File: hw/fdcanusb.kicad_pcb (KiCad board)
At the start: 4 copper layers, 30 x 18 mm, 33 parts, among them J1 Conn_01x03, J2 216990-0002, U1 STM32G474CEU6, U2 TCAN1057AEVDRQ1, U3 TLP3317, U4 USBLC6-2SC6, U5 TLV70233DSER

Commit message: WIP - nearly all routing complete
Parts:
- C2: moved to B.Cu
- moved C2 8.36 mm to (143.0, 105.5), turned to 90 degrees
- moved C6 7.94 mm to (139.8, 105.7)
- moved R1 7.31 mm to (143.8, 96.5)
- moved C7 6.12 mm to (137.3, 97.6), turned to 90 degrees
- moved U3 3.19 mm to (146.8, 98.8), turned to 0 degrees
- moved U1 2.76 mm to (134.3, 103.2), turned to 90 degrees
- moved C12 2.54 mm to (128.8, 99.5), turned to 180 degrees
- moved R2 2.30 mm to (146.8, 102.0)
- moved C3 2.23 mm to (128.8, 104.0), turned to 180 degrees
- moved R5 2.20 mm to (148.1, 93.7), turned to 180 degrees
- moved R6 2.19 mm to (148.2, 106.2), turned to 180 degrees
- moved C5 2.11 mm to (128.8, 101.0), turned to 180 degrees
- moved C4 1.88 mm to (128.8, 102.5), turned to 180 degrees
- moved D3 1.84 mm to (131.2, 92.3), turned to 0 degrees
- moved U4 1.24 mm to (130.3, 96.8)
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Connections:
- net Net-(J1-Pin_1) renamed /CAN/CAN_P
- net Net-(J1-Pin_2) renamed /CAN/CAN_N
- net Net-(J2-DN1) renamed /Power Input/USB_N
- net Net-(J2-DP1) renamed /Power Input/USB_P
- U1 pad 41: /stm32g4/LED_CAN_TX -> /LED Debug/LED_CAN_TX
- U1 pad 42: /stm32g4/LED_CAN_RX -> /LED Debug/LED_CAN_RX
- U1 pad 43: /stm32g4/LED_PWR -> /LED Debug/LED_PWR
- U1 pad 44: /stm32g4/LED_COM -> /LED Debug/LED_COM
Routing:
- net /LED Debug/LED_PWR: track 0.00 -> 43.1 mm, vias 0 -> 1
- net /LED Debug/LED_COM: track 0.00 -> 39.2 mm, vias 0 -> 1
- net +5V: track 0.00 -> 32.9 mm, vias 0 -> 1
- net GND: track 0.00 -> 31.3 mm, vias 0 -> 23
- net +3V: track 0.00 -> 23.7 mm, vias 0 -> 8
- net /CAN/CAN_TERM: track 0.00 -> 20.7 mm
- net /CAN/CAN_N: track 0.00 -> 17.0 mm, vias 0 -> 1
- net /CAN/CAN_P: track 0.00 -> 17.0 mm, vias 0 -> 1
- net /LED Debug/LED_CAN_TX: track 0.00 -> 16.3 mm, vias 0 -> 1
- net /stm32g4/NRST: track 0.00 -> 14.1 mm, vias 0 -> 2
- net /stm32g4/SWDIO: track 0.00 -> 13.9 mm, vias 0 -> 1
- net /Power Input/USB_N: track 0.00 -> 12.4 mm, vias 0 -> 2
- net /Power Input/USB_F_P: track 0.00 -> 11.7 mm, vias 0 -> 1
- net /Power Input/USB_P: track 0.00 -> 11.6 mm, vias 0 -> 2
- net /stm32g4/SWCLK: track 0.00 -> 11.4 mm, vias 0 -> 1
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- added copper zone on B.Cu, net GND
- added copper zone on F.Cu, net GND
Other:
- board text added: "SWD"

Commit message: Maybe complete routing and passes all DRC
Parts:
- moved C11 0.25 mm to (124.9, 97.5)
- moved D3 0.10 mm to (131.3, 92.3)
- moved R8 0.10 mm to (128.9, 93.6)
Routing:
- net +3V: track 23.7 -> 28.7 mm, vias 8 -> 12
- net GND: track 31.3 -> 34.3 mm, vias 23 -> 27
- added copper zone on F.Cu, net +3V
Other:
- board text added: "G"
- board text added: "H"
- board text added: "L"

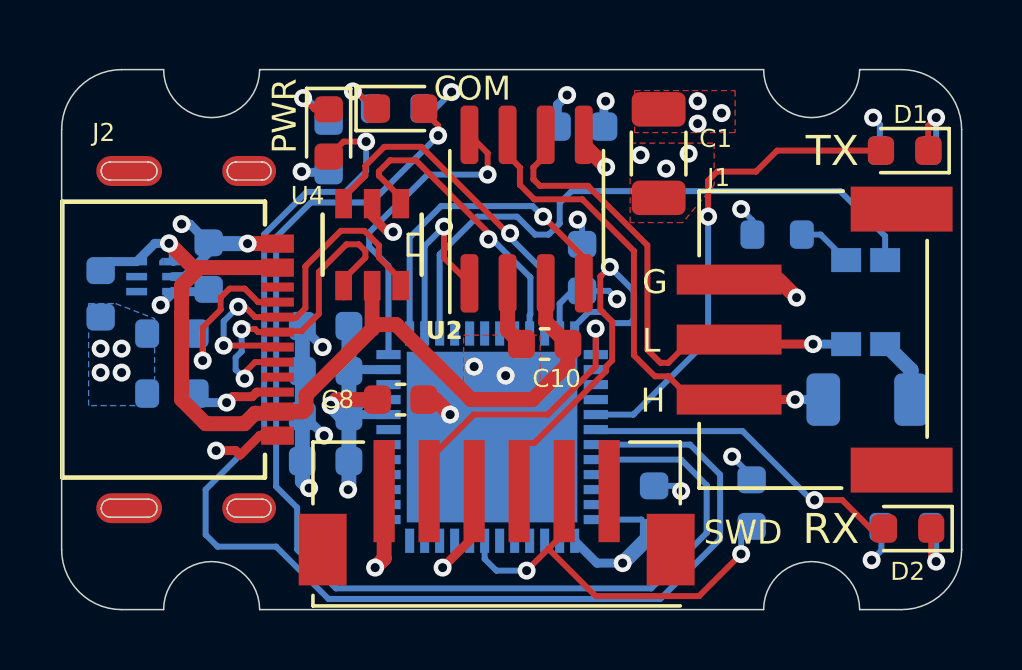
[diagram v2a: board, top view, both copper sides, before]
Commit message: r4: Add board label and fine silk tune
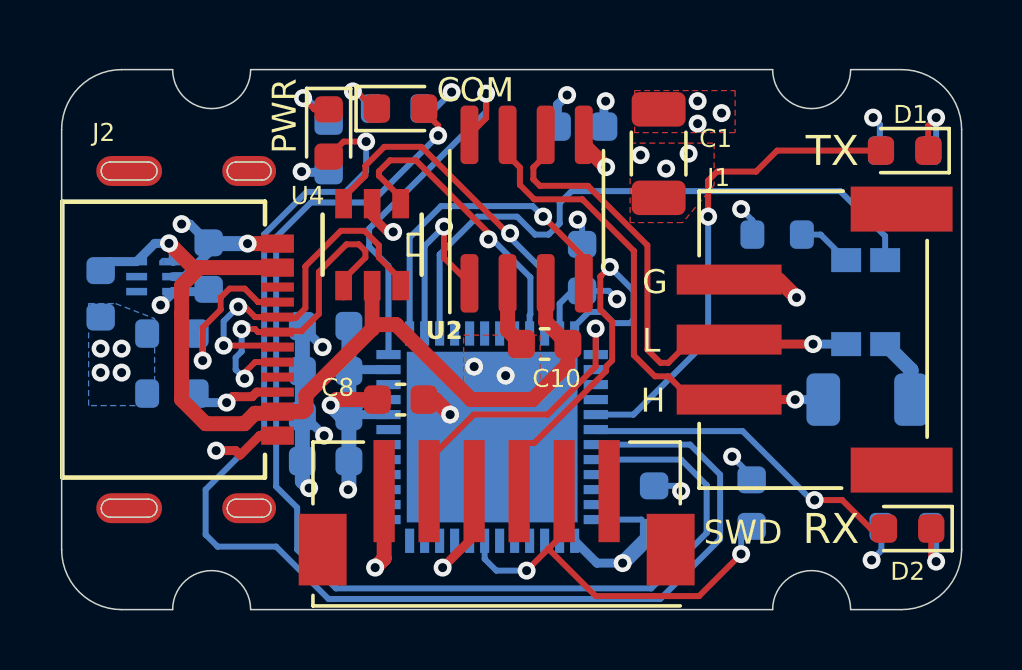
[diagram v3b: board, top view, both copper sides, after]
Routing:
- net /CAN/CAN_STB: track 10.7 -> 12.2 mm
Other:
- outline, holes or cut-outs redrawn
- board text added: "(c) 2023"
- board text added: "fdcanusb r4"

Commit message: r4: More work to get silk off vias
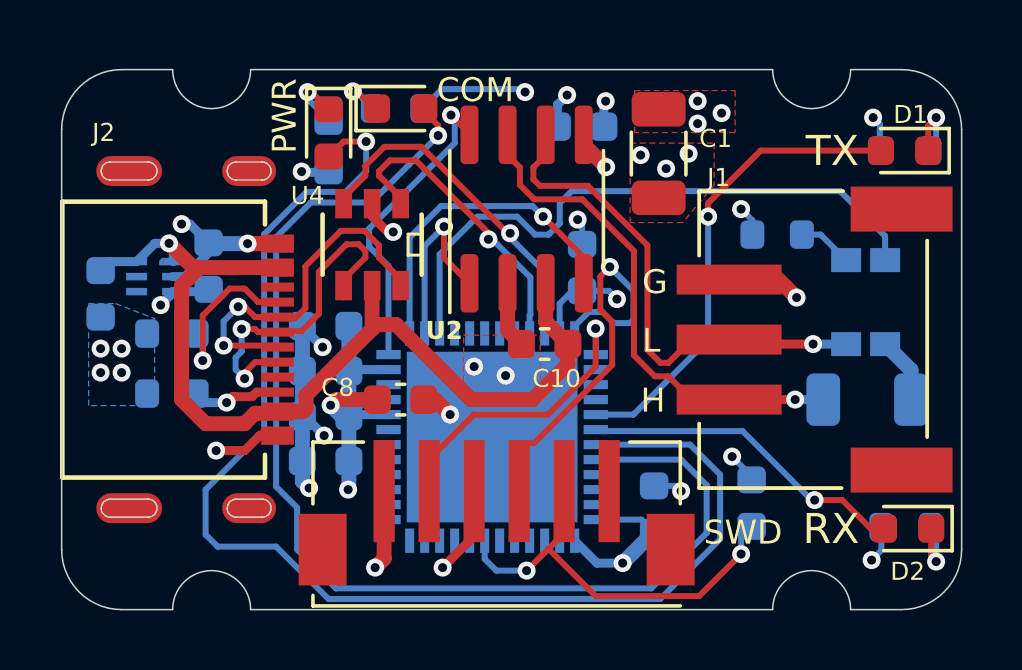
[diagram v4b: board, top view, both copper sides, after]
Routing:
- net GND: track 34.3 -> 36.7 mm
- net /CAN/CAN_STB: track 12.2 -> 10.4 mm

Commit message: Add debug pads for power rails
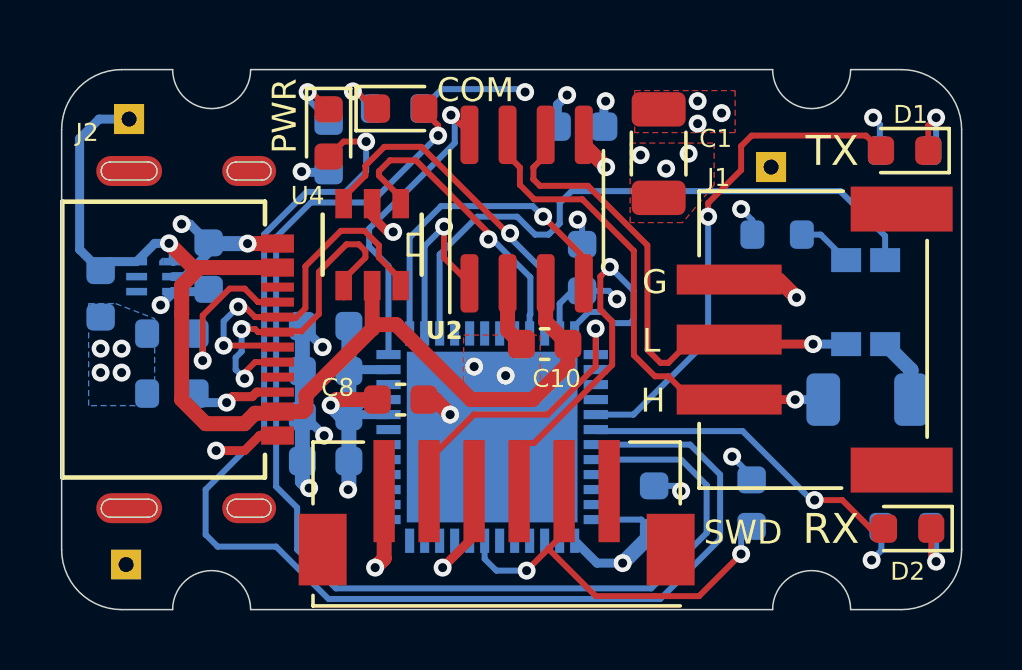
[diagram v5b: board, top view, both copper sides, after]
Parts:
- added J3: Conn_01x01, TestPoint:TestPoint_THTPad_1.0x1.0mm_Drill0.5mm, B.Cu at (122.2, 107.5)
- added J4: Conn_01x01, TestPoint:TestPoint_THTPad_1.0x1.0mm_Drill0.5mm, B.Cu at (143.7, 94.2)
- added J5: Conn_01x01, TestPoint:TestPoint_THTPad_1.0x1.0mm_Drill0.5mm, B.Cu at (122.2, 92.7)
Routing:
- net +5V: track 32.7 -> 39.4 mm
- net /LED Debug/LED_CAN_TX: track 15.8 -> 16.7 mm
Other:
- board text added: "3"
- board text added: "5"
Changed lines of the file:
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@@
     (property "ki_keywords" "216990-0002")
     (attr smd)
-    (fp_text reference "J2" (at -6.9 2 unlocked) (layer "F.SilkS")
+    (fp_text reference "J2" (at -6.9 2.55 unlocked) (layer "F.SilkS")
         (effects (font (size 0.6 0.6) (thickness 0.1)))
     )
@@
     )
   )
+  (footprint "TestPoint:TestPoint_THTPad_1.0x1.0mm_Drill0.5mm" (layer "B.Cu")
+    (at 143.65 94.25 180)
+    (descr "THT rectangular pad as test Point, square 1.0mm side length, hole diameter 0.5mm")
+    (tags "test point THT pad rectangle square")
+    (property "Sheetfile" "led_debug.kicad_sch")
+    (property "Sheetname" "LED Debug")
+    (property "exclude_from_bom" "")
+    (property "ki_description" "Generic connector, single row, 01x01, script generated (kicad-library-utils/schlib/autogen/connector/)")
+    (property "ki_keywords" "connector")
+    (attr exclude_from_pos_files exclude_from_bom)
+    (fp_text reference "J4" (at 0 1.448) (layer "B.SilkS") hide
+        (effects (font (size 1 1) (thickness 0.15)) (justify mirror))
+    )
+    (fp_text value "Conn_01x01" (at 0 -1.55) (layer "B.Fab") hide
+        (effects (font (size 1 1) (thickness 0.15)) (justify mirror))
+    )
+    (fp_line (start -0.7 -0.7) (end -0.7 0.7)
+      (stroke (width 0.12) (type solid)) (layer "B.SilkS"))
+    (fp_line (start -0.7 0.7) (end 0.7 0.7)
+      (stroke (width 0.12) (type solid)) (layer "B.SilkS"))
+    (fp_line (start 0.7 -0.7) (end -0.7 -0.7)
+      (stroke (width 0.12) (type solid)) (layer "B.SilkS"))
+    (fp_line (start 0.7 0.7) (end 0.7 -0.7)
+      (stroke (width 0.12) (type solid)) (layer "B.SilkS"))
+    (fp_line (start -1 1) (end -1 -1)
+      (stroke (width 0.05) (type solid)) (layer "B.CrtYd"))
+    (fp_line (start -1 1) (end 1 1)
+      (stroke (width 0.05) (type solid)) (layer "B.CrtYd"))
+    (fp_line (start 1 -1) (end -1 -1)
+      (stroke (width 0.05) (type solid)) (layer "B.CrtYd"))
+    (fp_line (start 1 -1) (end 1 1)
+      (stroke (width 0.05) (type solid)) (layer "B.CrtYd"))
+    (pad "1" thru_hole rect (at 0 0 180) (size 1 1) (drill 0.5) (layers "*.Cu" "*.Mask")
+      (net 1 "+3V") (pinfunction "Pin_1") (pintype "passive"))
+  )
+  (footprint "TestPoint:TestPoint_THTPad_1.0x1.0mm_Drill0.5mm" (layer "B.Cu")
+    (at 122.15 107.5 180)
+    (descr "THT rectangular pad as test Point, square 1.0mm side length, hole diameter 0.5mm")
+    (tags "test point THT pad rectangle square")
+    (property "Sheetfile" "led_debug.kicad_sch")
+    (property "Sheetname" "LED Debug")
+    (property "exclude_from_bom" "")
+    (property "ki_description" "Generic connector, single row, 01x01, script generated (kicad-library-utils/schlib/autogen/connector/)")
+    (property "ki_keywords" "connector")
+    (attr exclude_from_pos_files exclude_from_bom)
+    (fp_text reference "J3" (at 0 1.448) (layer "B.SilkS") hide
+        (effects (font (size 1 1) (thickness 0.15)) (justify mirror))
+    )
+    (fp_text value "Conn_01x01" (at 0 -1.55) (layer "B.Fab") hide
+        (effects (font (size 1 1) (thickness 0.15)) (justify mirror))
+    )
+    (fp_line (start -0.7 -0.7) (end -0.7 0.7)
+      (stroke (width 0.12) (type solid)) (layer "B.SilkS"))
+    (fp_line (start -0.7 0.7) (end 0.7 0.7)
+      (stroke (width 0.12) (type solid)) (layer "B.SilkS"))
+    (fp_line (start 0.7 -0.7) (end -0.7 -0.7)
+      (stroke (width 0.12) (type solid)) (layer "B.SilkS"))
+    (fp_line (start 0.7 0.7) (end 0.7 -0.7)
+      (stroke (width 0.12) (type solid)) (layer "B.SilkS"))
+    (fp_line (start -1 1) (end -1 -1)
+      (stroke (width 0.05) (type solid)) (layer "B.CrtYd"))
+    (fp_line (start -1 1) (end 1 1)
+      (stroke (width 0.05) (type solid)) (layer "B.CrtYd"))
+    (fp_line (start 1 -1) (end -1 -1)
+      (stroke (width 0.05) (type solid)) (layer "B.CrtYd"))
+    (fp_line (start 1 -1) (end 1 1)
+      (stroke (width 0.05) (type solid)) (layer "B.CrtYd"))
+    (pad "1" thru_hole rect (at 0 0 180) (size 1 1) (drill 0.5) (layers "*.Cu" "*.Mask")
+      (net 2 "GND") (pinfunction "Pin_1") (pintype "passive"))
+  )
   (footprint "Resistor_SMD:R_0603_1608Metric" (layer "B.Cu")
     (at 143.85 96.5)
@@
     )
   )
+  (footprint "TestPoint:TestPoint_THTPad_1.0x1.0mm_Drill0.5mm" (layer "B.Cu")
+    (at 122.25 92.65 180)
+    (descr "THT rectangular pad as test Point, square 1.0mm side length, hole diameter 0.5mm")
+    (tags "test point THT pad rectangle square")
+    (property "Sheetfile" "led_debug.kicad_sch")
+    (property "Sheetname" "LED Debug")
+    (property "exclude_from_bom" "")
+    (property "ki_description" "Generic connector, single row, 01x01, script generated (kicad-library-utils/schlib/autogen/connector/)")
+    (property "ki_keywords" "connector")
+    (attr exclude_from_pos_files exclude_from_bom)
+    (fp_text reference "J5" (at 0 1.448) (layer "B.SilkS") hide
+        (effects (font (size 1 1) (thickness 0.15)) (justify mirror))
+    )
+    (fp_text value "Conn_01x01" (at 0 -1.55) (layer "B.Fab") hide
+        (effects (font (size 1 1) (thickness 0.15)) (justify mirror))
+    )
+    (fp_line (start -0.7 -0.7) (end -0.7 0.7)
+      (stroke (width 0.12) (type solid)) (layer "B.SilkS"))
+    (fp_line (start -0.7 0.7) (end 0.7 0.7)
+      (stroke (width 0.12) (type solid)) (layer "B.SilkS"))
+    (fp_line (start 0.7 -0.7) (end -0.7 -0.7)
+      (stroke (width 0.12) (type solid)) (layer "B.SilkS"))
+    (fp_line (start 0.7 0.7) (end 0.7 -0.7)
+      (stroke (width 0.12) (type solid)) (layer "B.SilkS"))
+    (fp_line (start -1 1) (end -1 -1)
+      (stroke (width 0.05) (type solid)) (layer "B.CrtYd"))
+    (fp_line (start -1 1) (end 1 1)
+      (stroke (width 0.05) (type solid)) (layer "B.CrtYd"))
+    (fp_line (start 1 -1) (end -1 -1)
+      (stroke (width 0.05) (type solid)) (layer "B.CrtYd"))
+    (fp_line (start 1 -1) (end 1 1)
+      (stroke (width 0.05) (type solid)) (layer "B.CrtYd"))
+    (pad "1" thru_hole rect (at 0 0 180) (size 1 1) (drill 0.5) (layers "*.Cu" "*.Mask")
+      (net 4 "+5V") (pinfunction "Pin_1") (pintype "passive"))
+  )
   (footprint "Capacitor_SMD:C_0603_1608Metric" (layer "B.Cu")
     (at 128.8 104.05 180)
@@
   (gr_line (start 126.3 91) (end 143.7 91)
     (stroke (width 0.05) (type default)) (layer "Edge.Cuts"))
+  (gr_text "G" (at 124.1 107.75) (layer "B.SilkS")
+    (effects (font (size 0.8 0.8) (thickness 0.125)) (justify left bottom mirror))
+  )
+  (gr_text "3" (at 145.6 94.75) (layer "B.SilkS")
+    (effects (font (size 0.8 0.8) (thickness 0.125)) (justify left bottom mirror))
+  )
   (gr_text "(c) 2023" (at 133.7 97.75) (layer "B.SilkS")
     (effects (font (size 0.8 0.8) (thickness 0.125)) (justify left bottom mirror))
@@
     (effects (font (size 0.8 0.8) (thickness 0.125)) (justify left bottom mirror))
   )
+  (gr_text "5" (at 124.15 93.2) (layer "B.SilkS")
+    (effects (font (size 0.8 0.8) (thickness 0.125)) (justify left bottom mirror))
+  )
   (gr_text "G" (at 139.35 98.55) (layer "F.SilkS")
     (effects (font (size 0.8 0.8) (thickness 0.125)) (justify left bottom))
@@
   (segment (start 121.599998 97.400002) (end 121.3 97.7) (width 0.3) (layer "B.Cu") (net 4))
   (segment (start 123.720002 97.400002) (end 123.720002 96.931164) (width 0.3) (layer "B.Cu") (net 4))
+  (segment (start 120.6 97) (end 120.6 93.3) (width 0.3) (layer "B.Cu") (net 4))
+  (segment (start 120.6 93.3) (end 121.25 92.65) (width 0.3) (layer "B.Cu") (net 4))
+  (segment (start 121.3 97.7) (end 120.6 97) (width 0.3) (layer "B.Cu") (net 4))
+  (segment (start 121.25 92.65) (end 122.25 92.65) (width 0.3) (layer "B.Cu") (net 4))
   (segment (start 148.8875 92.8625) (end 149.15 92.6) (width 0.2) (layer "F.Cu") (net 5))
   (segment (start 148.8875 93.7) (end 148.8875 92.8625) (width 0.2) (layer "F.Cu") (net 5))
@@
   (segment (start 149.15 93.475) (end 148.925 93.7) (width 0.2) (layer "B.Cu") (net 5))
   (segment (start 149.15 92.6) (end 149.15 93.475) (width 0.2) (layer "B.Cu") (net 5))
-  (segment (start 141.55 95.45) (end 143.3 93.7) (width 0.2) (layer "F.Cu") (net 6))
+  (segment (start 146.8125 93.2) (end 147.3125 93.7) (width 0.2) (layer "F.Cu") (net 6))
+  (segment (start 142.65 93.55) (end 143 93.2) (width 0.2) (layer "F.Cu") (net 6))
+  (segment (start 143 93.2) (end 146.8125 93.2) (width 0.2) (layer "F.Cu") (net 6))
   (segment (start 141.55 95.9) (end 141.55 95.45) (width 0.2) (layer "F.Cu") (net 6))
-  (segment (start 143.3 93.7) (end 147.3125 93.7) (width 0.2) (layer "F.Cu") (net 6))
+  (segment (start 142.65 94.35) (end 142.65 93.55) (width 0.2) (layer "F.Cu") (net 6))
+  (segment (start 141.55 95.45) (end 142.65 94.35) (width 0.2) (layer "F.Cu") (net 6))
   (via (at 141.55 95.9) (size 0.6) (drill 0.3) (layers "F.Cu" "B.Cu") (net 6))
   (segment (start 141.55 100.010799) (end 141.55 95.9) (width 0.2) (layer "B.Cu") (net 6))
